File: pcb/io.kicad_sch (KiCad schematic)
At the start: 1 part, among them J3 650913-5

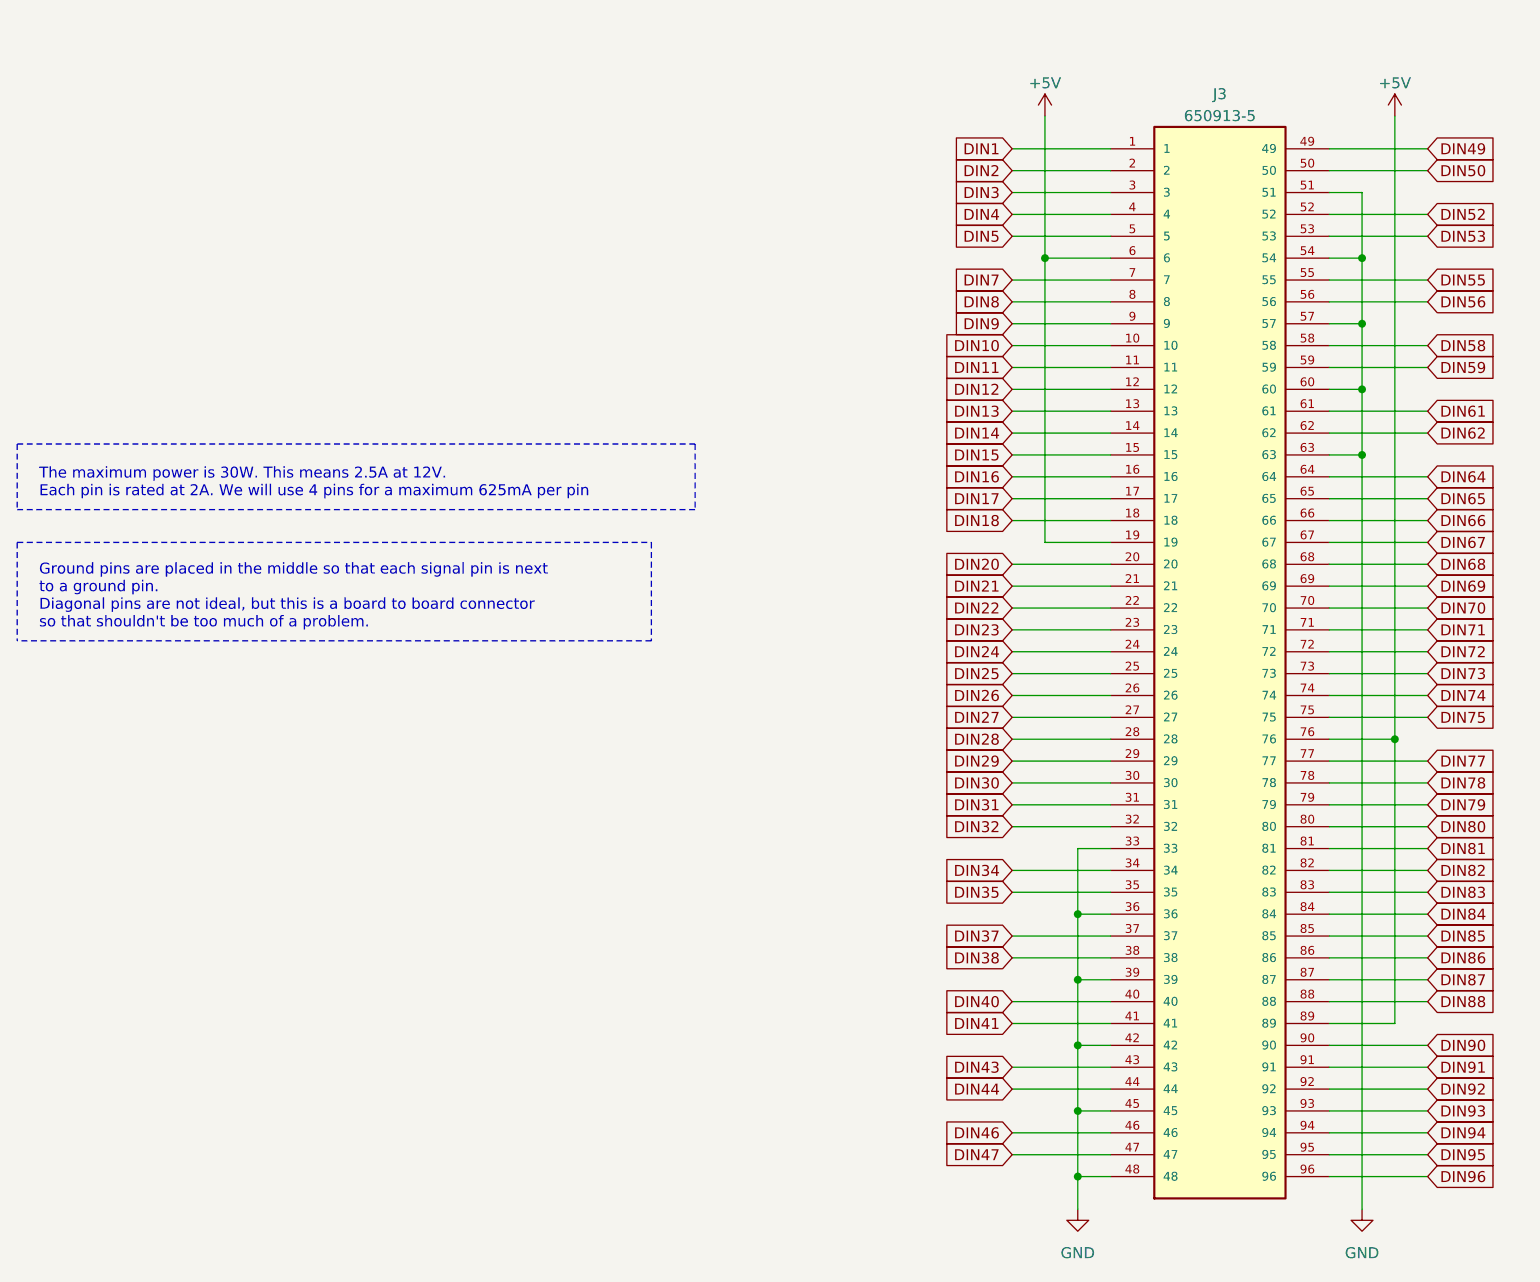
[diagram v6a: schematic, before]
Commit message: edit the connector pinout
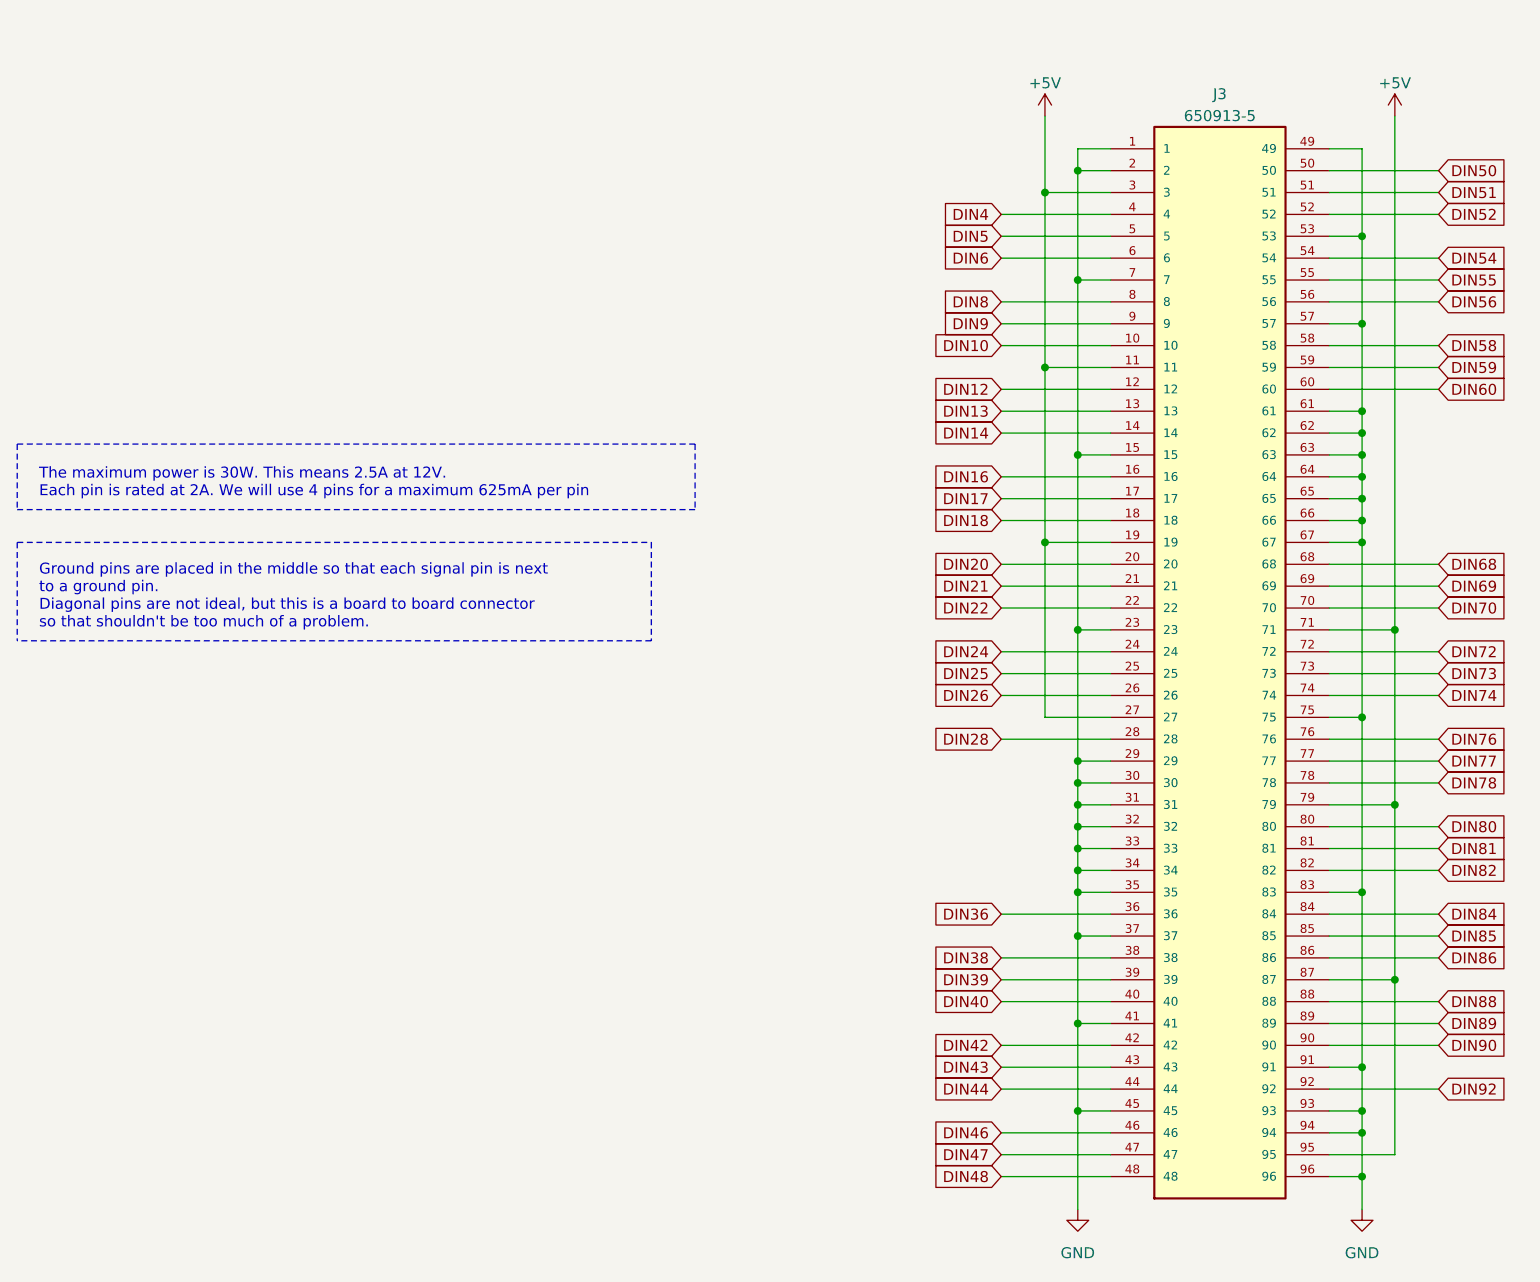
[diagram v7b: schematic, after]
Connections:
- net DIN1 is gone; now on net GND: J3.1
- net DIN11 is gone; now on net +5V: J3.11
- net DIN15 is gone; now on net GND: J3.15
- net DIN2 is gone; now on net GND: J3.2
- net DIN23 is gone; now on net GND: J3.23
- net DIN27 is gone; now on net +5V: J3.27
- net DIN29 is gone; now on net GND: J3.29
- net DIN3 is gone; now on net +5V: J3.3
- net DIN30 is gone; now on net GND: J3.30
- net DIN31 is gone; now on net GND: J3.31
- net DIN32 is gone; now on net GND: J3.32
- net DIN34 is gone; now on net GND: J3.34
- net DIN35 is gone; now on net GND: J3.35
- net DIN37 is gone; now on net GND: J3.37
- net DIN41 is gone; now on net GND: J3.41
- net DIN49 is gone; now on net GND: J3.49
- net DIN53 is gone; now on net GND: J3.53
- net DIN61 is gone; now on net GND: J3.61
- net DIN62 is gone; now on net GND: J3.62
- net DIN64 is gone; now on net GND: J3.64
- net DIN65 is gone; now on net GND: J3.65
- net DIN66 is gone; now on net GND: J3.66
- net DIN67 is gone; now on net GND: J3.67
- net DIN7 is gone; now on net GND: J3.7
- net DIN71 is gone; now on net +5V: J3.71
- net DIN75 is gone; now on net GND: J3.75
- net DIN79 is gone; now on net +5V: J3.79
- net DIN83 is gone; now on net GND: J3.83
- net DIN87 is gone; now on net +5V: J3.87
- net DIN91 is gone; now on net GND: J3.91
- net DIN93 is gone; now on net GND: J3.93
- net DIN94 is gone; now on net GND: J3.94
- net DIN95 is gone; now on net +5V: J3.95
- net DIN96 is gone; now on net GND: J3.96
- net +5V: no longer J3.6, J3.76, J3.89
- net GND: no longer J3.36, J3.39, J3.42, J3.48, J3.51, J3.54, J3.60
- new net DIN36: J3.36
- new net DIN39: J3.39
- new net DIN42: J3.42
- new net DIN48: J3.48
- new net DIN51: J3.51
- new net DIN54: J3.54
- new net DIN6: J3.6
- new net DIN60: J3.60
- new net DIN76: J3.76
- new net DIN89: J3.89
